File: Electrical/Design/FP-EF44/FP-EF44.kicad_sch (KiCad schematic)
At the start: 17 parts

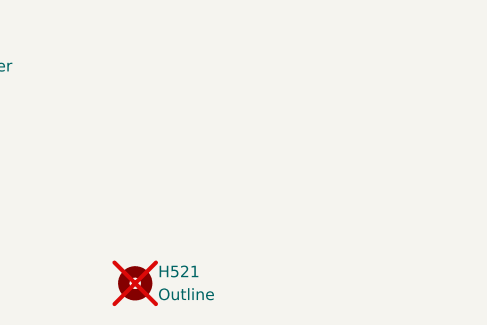
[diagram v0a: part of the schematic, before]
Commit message: SUKU frontpanel hatch pattern updated, outline updated, silk screen updated
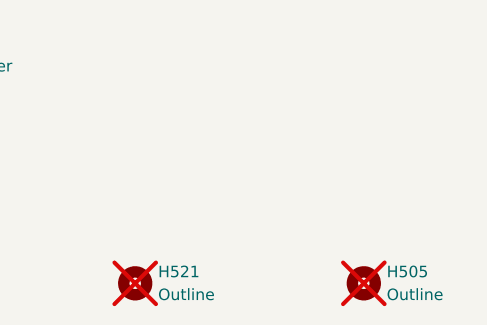
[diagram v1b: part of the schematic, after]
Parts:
- added H505: Outline, suku_basics:OSHWA, symbol Mechanical:MountingHole
- H521: footprint suku_basics:FP_OUTLINE -> suku_basics:FP_OUTLINE_2
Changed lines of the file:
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@@
+	(symbol
+		(lib_id "Mechanical:MountingHole")
+		(at 177.8 177.8 0)
+		(unit 1)
+		(exclude_from_sim yes)
+		(in_bom no)
+		(on_board yes)
+		(dnp yes)
+		(fields_autoplaced yes)
+		(property "Reference" "H505"
+			(at 180.34 176.5299 0)
+			(effects
+				(font
+					(size 1.27 1.27)
+				)
+				(justify left)
+			)
+		)
+		(property "Value" "Outline"
+			(at 180.34 179.0699 0)
+			(effects
+				(font
+					(size 1.27 1.27)
+				)
+				(justify left)
+			)
+		)
+		(property "Footprint" "suku_basics:OSHWA"
+			(at 177.8 177.8 0)
+			(effects
+				(font
+					(size 1.27 1.27)
+				)
+				(hide yes)
+			)
+		)
+		(property "Datasheet" "~"
+			(at 177.8 177.8 0)
+			(effects
+				(font
+					(size 1.27 1.27)
+				)
+				(hide yes)
+			)
+		)
+		(property "Description" "Mounting Hole without connection"
+			(at 177.8 177.8 0)
+			(effects
+				(font
+					(size 1.27 1.27)
+				)
+				(hide yes)
+			)
+		)
+		(instances
+			(project "FP-EF44"
+				(path "/e5217a0c-7f55-4c30-adda-7f8d95709d1b"
+					(reference "H505")
+					(unit 1)
+				)
+			)
+		)
+	)
 	(symbol
 		(lib_id "Mechanical:MountingHole")
@@
 			)
 		)
-		(property "Footprint" "suku_basics:FP_OUTLINE"
+		(property "Footprint" "suku_basics:FP_OUTLINE_2"
 			(at 152.4 177.8 0)
 			(effects

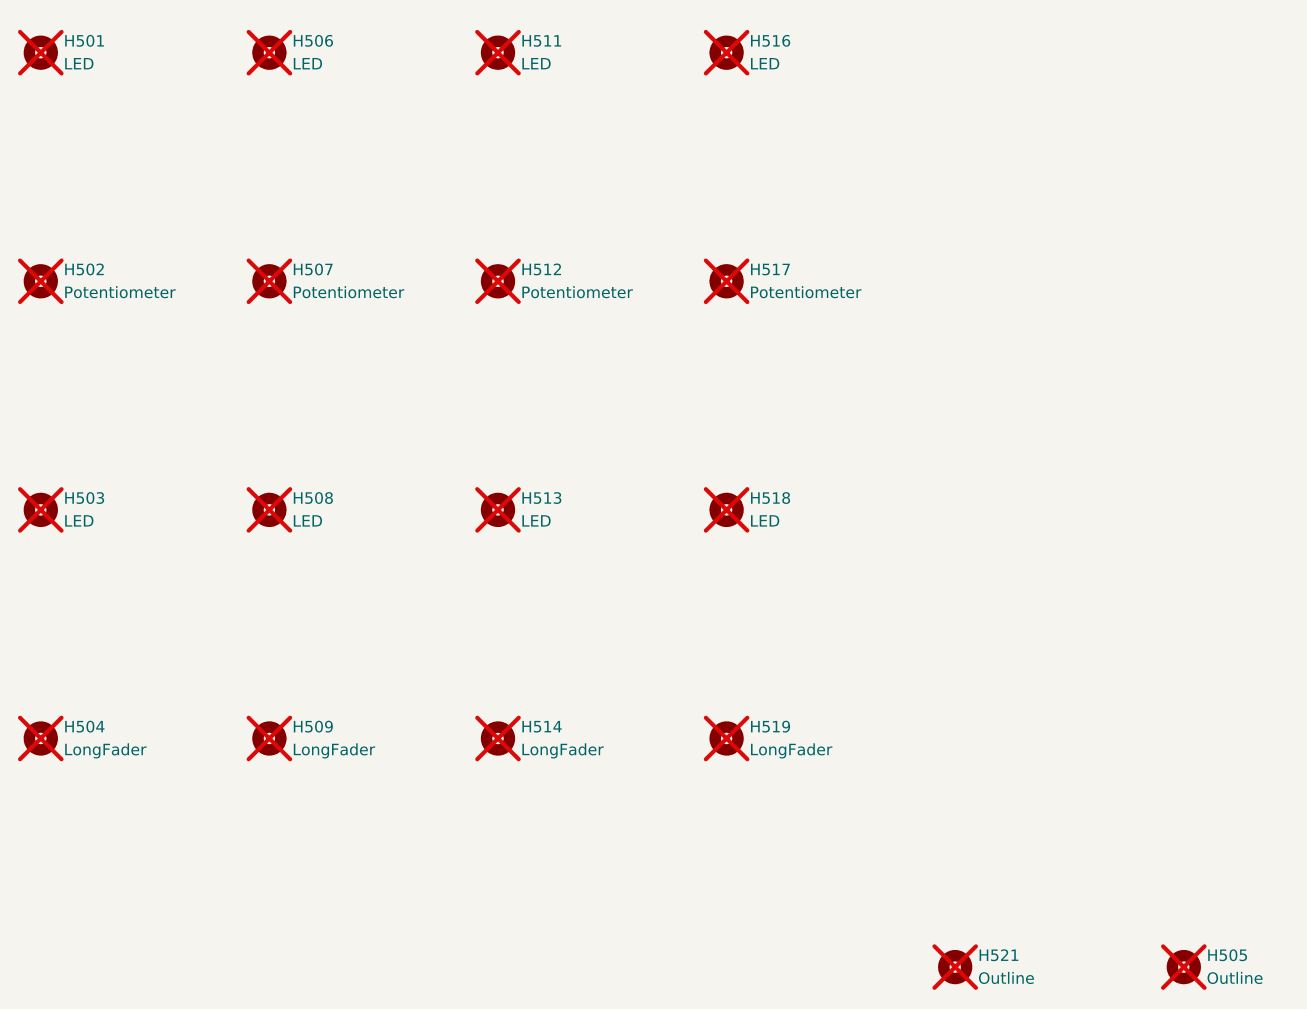
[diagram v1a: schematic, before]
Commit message: SUKU rest of the frontpanels updated to use the plated through-hole for lightpipe
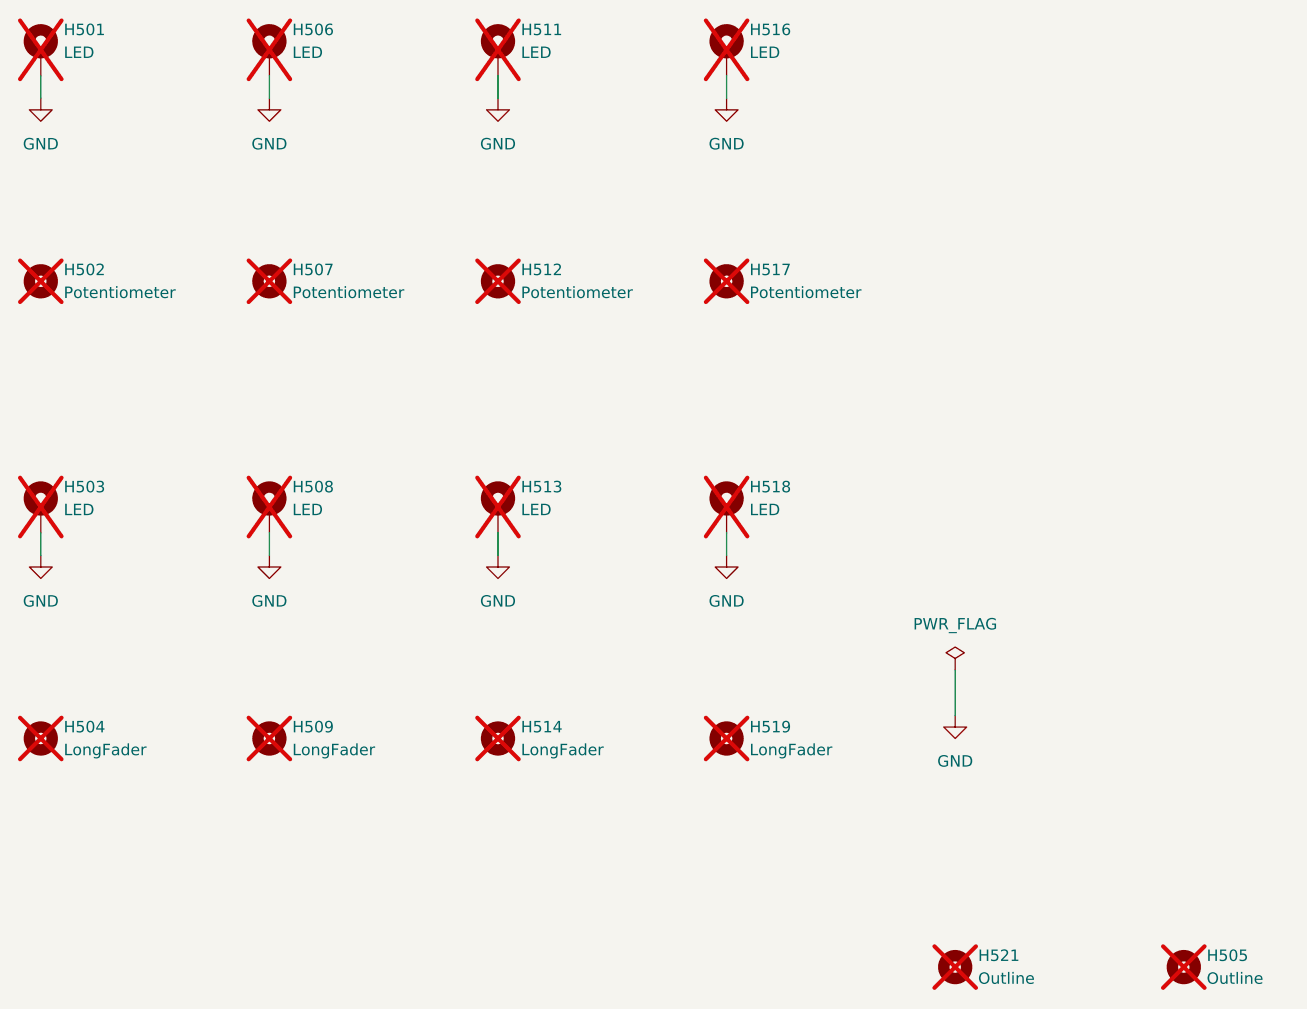
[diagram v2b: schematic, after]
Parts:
- H501, H503, H506, H508, H511, H513, H516, H518: footprint suku_basics:FP_LED -> suku_basics:FP_LED_TIGHT; symbol Mechanical:MountingHole -> Mechanical:MountingHole_Pad
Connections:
- new net GND: H501.1, H503.1, H506.1, H508.1, H511.1, H513.1, H516.1, H518.1
